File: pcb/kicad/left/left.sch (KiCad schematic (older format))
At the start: 61 parts, among them J1 USB_C_Receptacle_USB2.0, J2 AudioJack4, J3 Conn_01x12_Male, SW1 BOOT, SW10 SW_Push, SW12 SW_Push, SW13 SW_Push, SW14 SW_Push, SW15 SW_Push, SW17 SW_Push, SW18 SW_Push, SW19 SW_Push, SW2 RESET, SW21 SW_Push, SW22 SW_Push, SW23 SW_Push, SW24 SW_Push, SW3 SW_Push, SW31 SW_Push, SW32 SW_Push, SW33 SW_Push, SW34 SW_Push, SW4 SW_Push, SW5 SW_Push, SW7 SW_Push, SW8 SW_Push, SW9 SW_Push, U1 STM32, U2 LDO

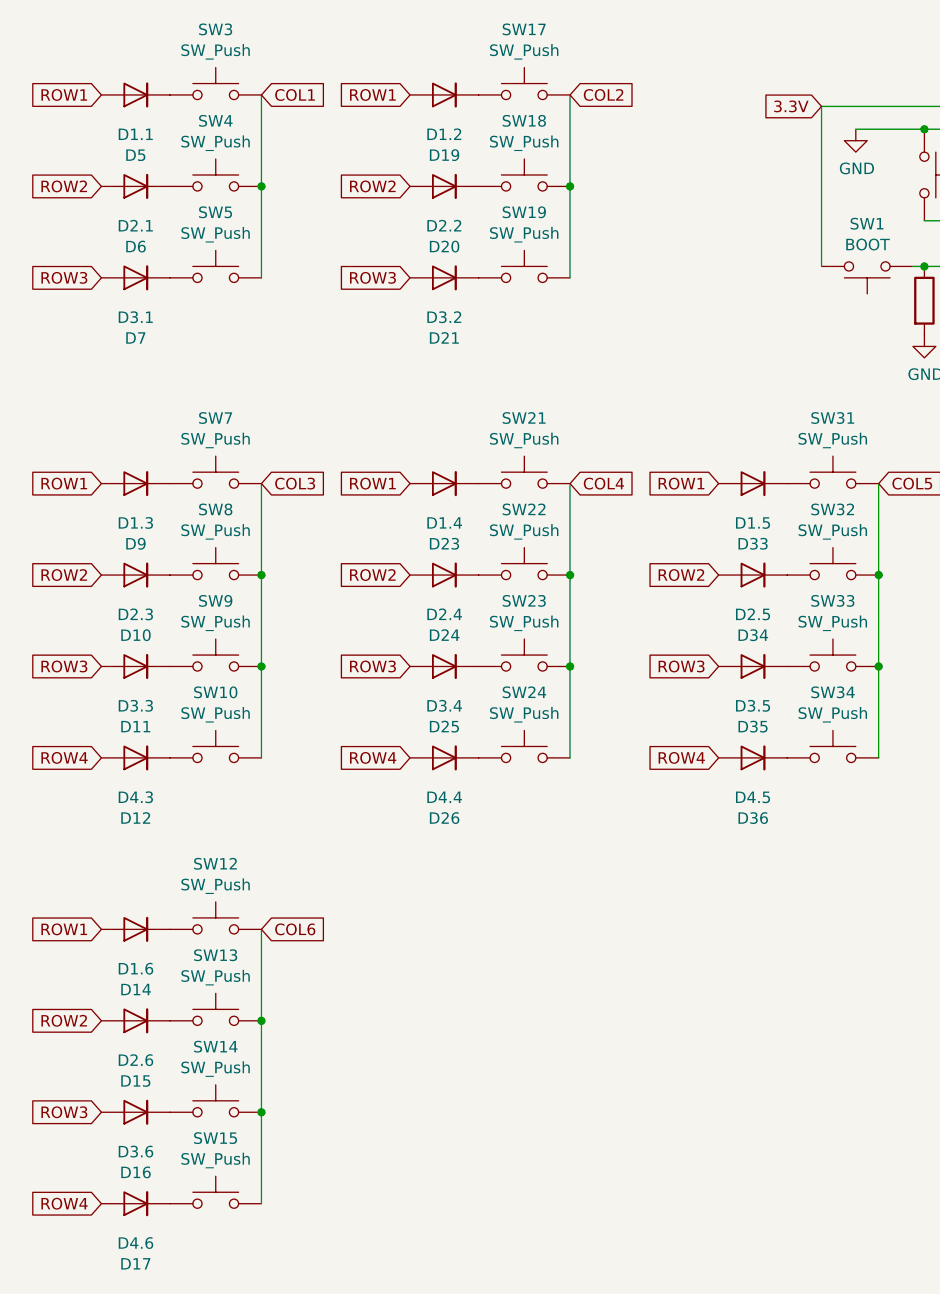
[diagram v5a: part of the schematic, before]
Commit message: Fix diode orientation
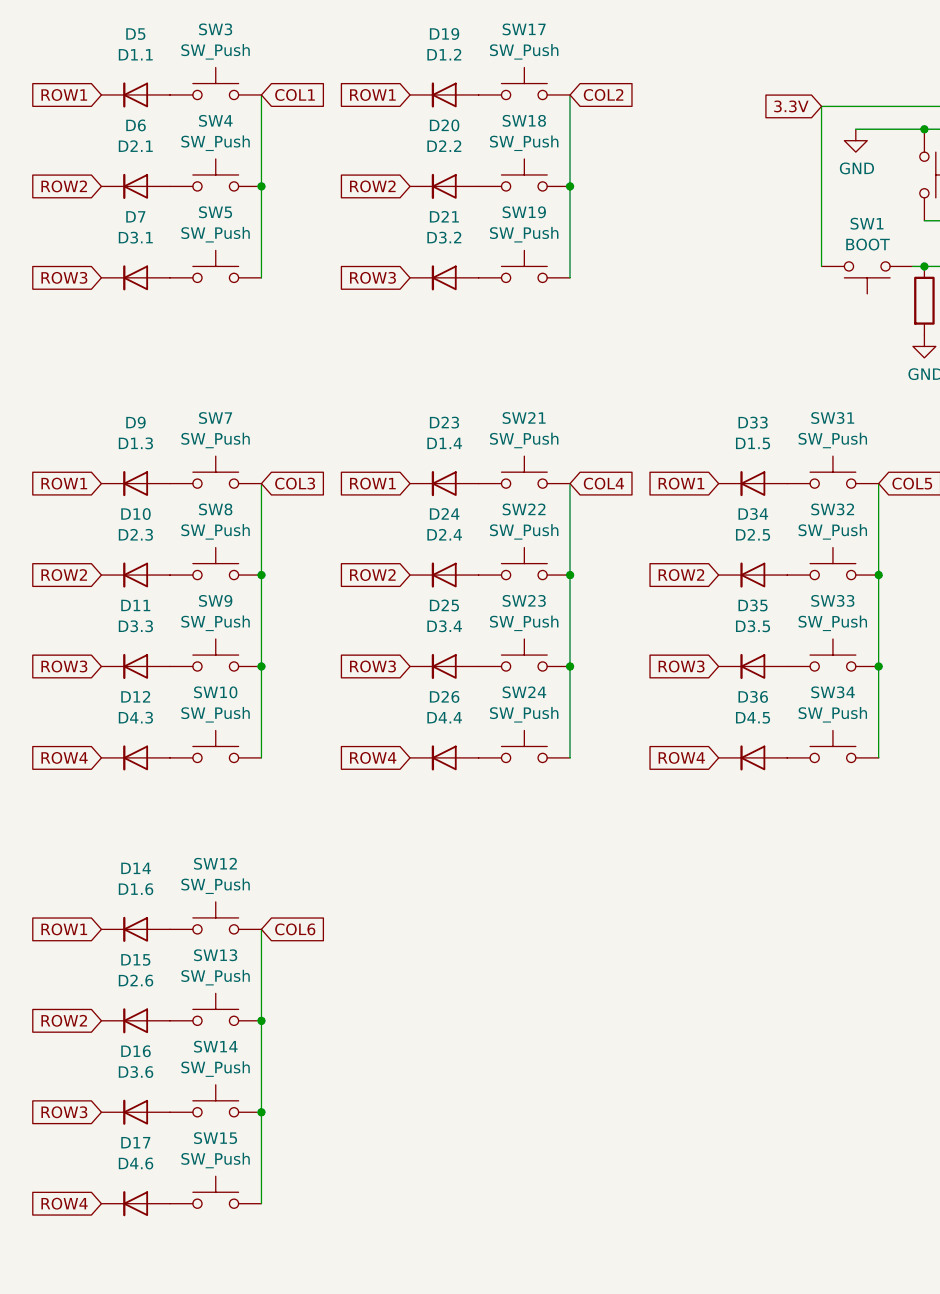
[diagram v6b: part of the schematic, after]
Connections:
- net ROW1: now also D14.1 (K), D19.1 (K), D23.1 (K), D33.1 (K), D5.1 (K), D9.1 (K); no longer D14.2 (A), D19.2 (A), D23.2 (A), D33.2 (A), D5.2 (A), D9.2 (A)
- net ROW2: now also D10.1 (K), D15.1 (K), D20.1 (K), D24.1 (K), D34.1 (K), D6.1 (K); no longer D10.2 (A), D15.2 (A), D20.2 (A), D24.2 (A), D34.2 (A), D6.2 (A)
- net ROW3: now also D11.1 (K), D16.1 (K), D21.1 (K), D25.1 (K), D35.1 (K), D7.1 (K); no longer D11.2 (A), D16.2 (A), D21.2 (A), D25.2 (A), D35.2 (A), D7.2 (A)
- net ROW4: now also D12.1 (K), D17.1 (K), D26.1 (K), D36.1 (K); no longer D12.2 (A), D17.2 (A), D26.2 (A), D36.2 (A)
- net at SW9.1: now also D11.2 (A); no longer D11.1 (K)
- net at SW10.1: now also D12.2 (A); no longer D12.1 (K)
- net at SW8.1: now also D10.2 (A); no longer D10.1 (K)
- net at SW7.1: now also D9.2 (A); no longer D9.1 (K)
- net at SW23.1: now also D25.2 (A); no longer D25.1 (K)
- net at SW24.1: now also D26.2 (A); no longer D26.1 (K)
- net at SW22.1: now also D24.2 (A); no longer D24.1 (K)
- net at SW21.1: now also D23.2 (A); no longer D23.1 (K)
- net at SW33.1: now also D35.2 (A); no longer D35.1 (K)
- net at SW34.1: now also D36.2 (A); no longer D36.1 (K)
- net at SW32.1: now also D34.2 (A); no longer D34.1 (K)
- net at SW31.1: now also D33.2 (A); no longer D33.1 (K)
- net at SW5.1: now also D7.2 (A); no longer D7.1 (K)
- net at SW4.1: now also D6.2 (A); no longer D6.1 (K)
- net at SW3.1: now also D5.2 (A); no longer D5.1 (K)
- net at SW19.1: now also D21.2 (A); no longer D21.1 (K)
- net at SW18.1: now also D20.2 (A); no longer D20.1 (K)
- net at SW17.1: now also D19.2 (A); no longer D19.1 (K)
- net at SW14.1: now also D16.2 (A); no longer D16.1 (K)
- net at SW15.1: now also D17.2 (A); no longer D17.1 (K)
- net at SW13.1: now also D15.2 (A); no longer D15.1 (K)
- net at SW12.1: now also D14.2 (A); no longer D14.1 (K)
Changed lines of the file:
@@
 F 3 "~" H 1000 3350 50  0001 C CNN
 	1    1000 3350
-	-1   0    0    1
+	1    0    0    -1
 $EndComp
 $Comp
@@
 F 3 "~" H 1000 3750 50  0001 C CNN
 	1    1000 3750
-	-1   0    0    1
+	1    0    0    -1
 $EndComp
 $Comp
@@
 F 3 "~" H 1000 2950 50  0001 C CNN
 	1    1000 2950
-	-1   0    0    1
+	1    0    0    -1
 $EndComp
 $Comp
@@
 F 3 "~" H 1000 2550 50  0001 C CNN
 	1    1000 2550
-	-1   0    0    1
+	1    0    0    -1
 $EndComp
 $Comp
@@
 F 3 "~" H 2350 3350 50  0001 C CNN
 	1    2350 3350
-	-1   0    0    1
+	1    0    0    -1
 $EndComp
 $Comp
@@
 F 3 "~" H 2350 3750 50  0001 C CNN
 	1    2350 3750
-	-1   0    0    1
+	1    0    0    -1
 $EndComp
 $Comp
@@
 F 3 "~" H 2350 2950 50  0001 C CNN
 	1    2350 2950
-	-1   0    0    1
+	1    0    0    -1
 $EndComp
 $Comp
@@
 F 3 "~" H 2350 2550 50  0001 C CNN
 	1    2350 2550
-	-1   0    0    1
+	1    0    0    -1
 $EndComp
 $Comp
@@
 F 3 "~" H 3700 3350 50  0001 C CNN
 	1    3700 3350
-	-1   0    0    1
+	1    0    0    -1
 $EndComp
 $Comp
@@
 F 3 "~" H 3700 3750 50  0001 C CNN
 	1    3700 3750
-	-1   0    0    1
+	1    0    0    -1
 $EndComp
 $Comp
@@
 F 3 "~" H 3700 2950 50  0001 C CNN
 	1    3700 2950
-	-1   0    0    1
+	1    0    0    -1
 $EndComp
 $Comp
@@
 F 3 "~" H 3700 2550 50  0001 C CNN
 	1    3700 2550
-	-1   0    0    1
+	1    0    0    -1
 $EndComp
 $Comp
@@
 F 3 "~" H 1000 1650 50  0001 C CNN
 	1    1000 1650
-	-1   0    0    1
+	1    0    0    -1
 $EndComp
 $Comp
@@
 F 3 "~" H 1000 1250 50  0001 C CNN
 	1    1000 1250
-	-1   0    0    1
+	1    0    0    -1
 $EndComp
 $Comp
@@
 F 3 "~" H 1000 850 50  0001 C CNN
 	1    1000 850
-	-1   0    0    1
+	1    0    0    -1
 $EndComp
 $Comp
@@
 F 3 "~" H 2350 1650 50  0001 C CNN
 	1    2350 1650
-	-1   0    0    1
+	1    0    0    -1
 $EndComp
 $Comp
@@
 F 3 "~" H 2350 1250 50  0001 C CNN
 	1    2350 1250
-	-1   0    0    1
+	1    0    0    -1
 $EndComp
 $Comp
@@
 F 3 "~" H 2350 850 50  0001 C CNN
 	1    2350 850
-	-1   0    0    1
+	1    0    0    -1
 $EndComp
 $Comp
@@
 F 3 "~" H 1000 5300 50  0001 C CNN
 	1    1000 5300
-	-1   0    0    1
+	1    0    0    -1
 $EndComp
 $Comp
@@
 F 3 "~" H 1000 5700 50  0001 C CNN
 	1    1000 5700
-	-1   0    0    1
+	1    0    0    -1
 $EndComp
 $Comp
@@
 F 3 "~" H 1000 4900 50  0001 C CNN
 	1    1000 4900
-	-1   0    0    1
+	1    0    0    -1
 $EndComp
 $Comp
@@
 F 3 "~" H 1000 4500 50  0001 C CNN
 	1    1000 4500
-	-1   0    0    1
-$EndComp
-$Comp
+	1    0    0    -1
+$EndComp
+$Comp
